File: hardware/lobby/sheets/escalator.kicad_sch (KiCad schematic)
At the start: 2 parts

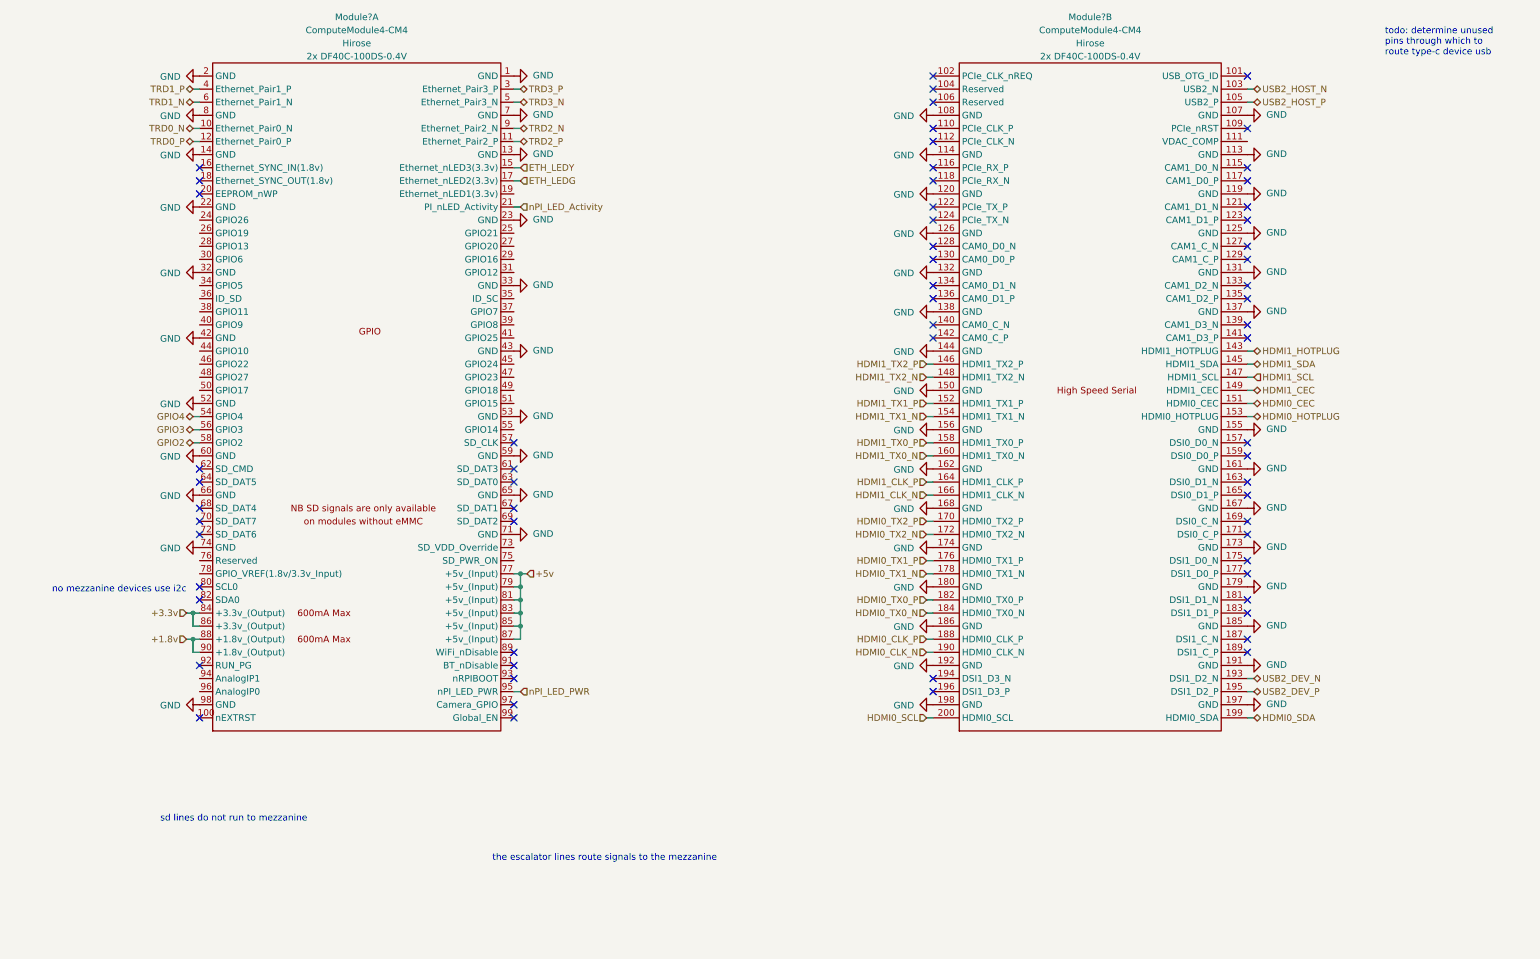
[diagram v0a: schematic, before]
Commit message: start routing mezzanine
making a progress capture before trying to cram a lot of signals onto just one hirose connector...
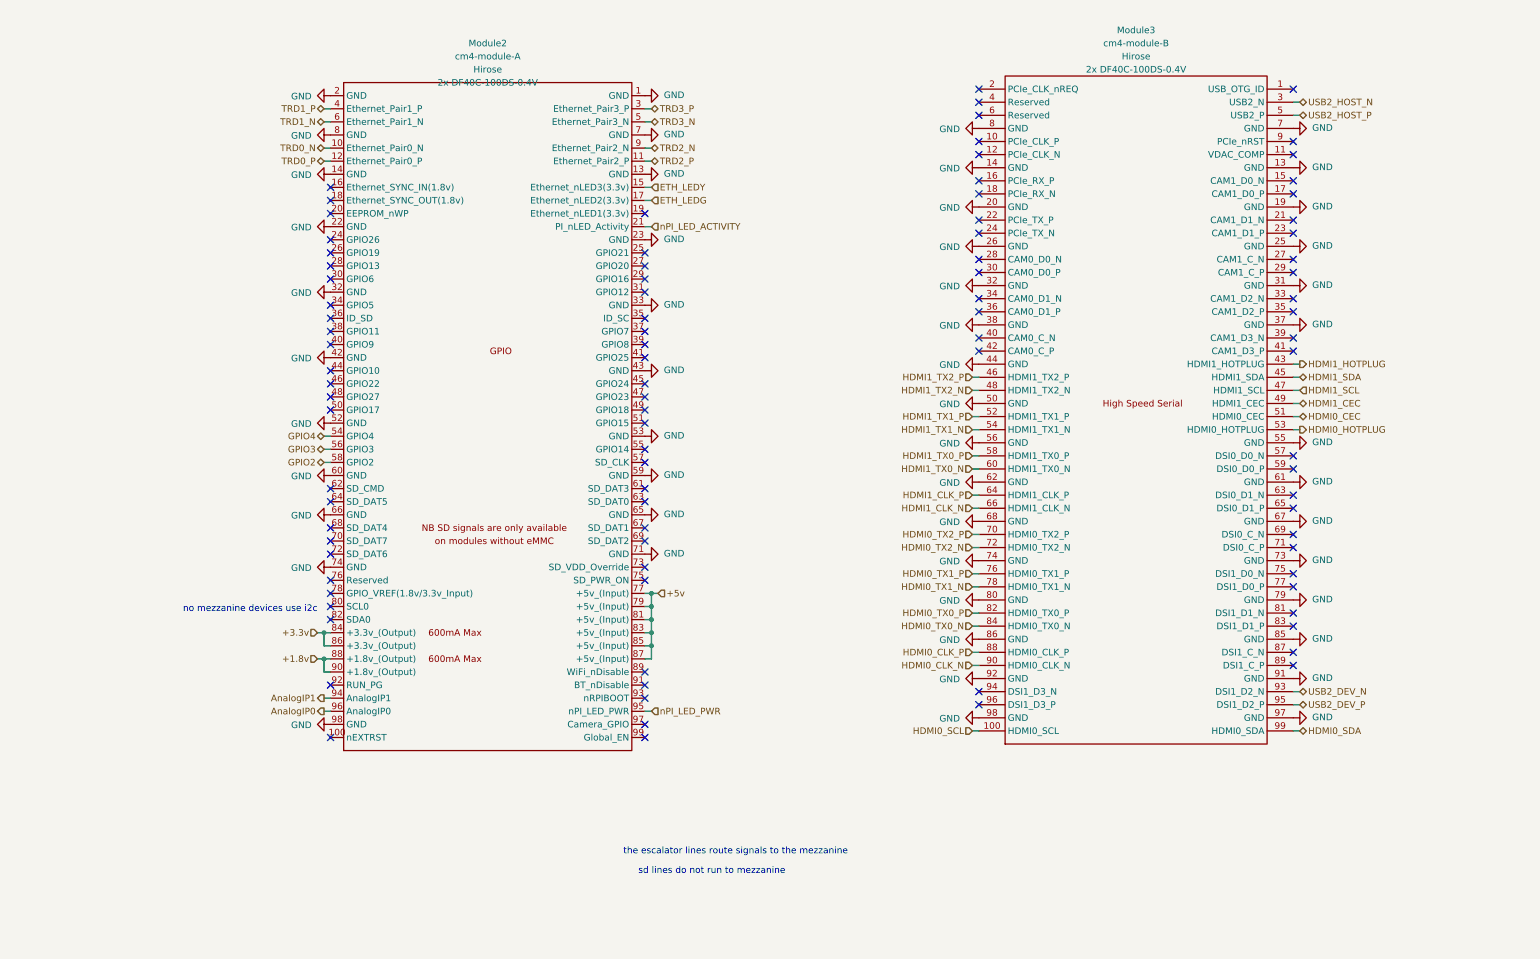
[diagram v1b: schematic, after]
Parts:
- removed Module? (x2): ComputeModule4-CM4, cm4crypto:DF40C-100DS-0.4V(51), symbol cm4crypto:ComputeModule4-CM4
- added Module2: cm4-module-A, cm4crypto:DF40C-100DS-0.4V(51), symbol cm4crypto:cm4-module-A
- added Module3: cm4-module-B, cm4crypto:DF40C-100DS-0.4V(51), symbol cm4crypto:cm4-module-B
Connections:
- net +1.8v: now also Module2.88 (+1.8v_(Output)), Module2.90 (+1.8v_(Output))
- net +3.3v: now also Module2.84 (+3.3v_(Output)), Module2.86 (+3.3v_(Output))
- net +5v: now also Module2.77 (+5v_(Input)), Module2.79 (+5v_(Input)), Module2.81 (+5v_(Input)), Module2.83 (+5v_(Input)), Module2.85 (+5v_(Input)), Module2.87 (+5v_(Input))
- net ETH_LEDG: now also Module2.17 (Ethernet_nLED2(3.3v))
- net ETH_LEDY: now also Module2.15 (Ethernet_nLED3(3.3v))
- net GND: now also Module2.1 (GND), Module2.13 (GND), Module2.14 (GND), Module2.2 (GND), Module2.22 (GND), Module2.23 (GND), Module2.32 (GND), Module2.33 (GND), Module2.42 (GND), Module2.43 (GND), Module2.52 (GND), Module2.53 (GND), Module2.59 (GND), Module2.60 (GND), Module2.65 (GND), Module2.66 (GND), Module2.7 (GND), Module2.71 (GND), Module2.74 (GND), Module2.8 (GND), Module2.98 (GND), Module3.13 (GND), Module3.14 (GND), Module3.19 (GND), Module3.20 (GND), Module3.25 (GND), Module3.26 (GND), Module3.31 (GND), Module3.32 (GND), Module3.37 (GND), Module3.38 (GND), Module3.44 (GND), Module3.50 (GND), Module3.55 (GND), Module3.56 (GND), Module3.61 (GND), Module3.62 (GND), Module3.67 (GND), Module3.68 (GND), Module3.7 (GND), Module3.73 (GND), Module3.74 (GND), Module3.79 (GND), Module3.8 (GND), Module3.80 (GND), Module3.85 (GND), Module3.86 (GND), Module3.91 (GND), Module3.92 (GND), Module3.97 (GND), Module3.98 (GND)
- net GPIO2: now also Module2.58 (GPIO2)
- net GPIO3: now also Module2.56 (GPIO3)
- net GPIO4: now also Module2.54 (GPIO4)
- net HDMI0_CEC: now also Module3.51 (HDMI0_CEC)
- net HDMI0_CLK_N: now also Module3.90 (HDMI0_CLK_N)
- net HDMI0_CLK_P: now also Module3.88 (HDMI0_CLK_P)
- net HDMI0_HOTPLUG: now also Module3.53 (HDMI0_HOTPLUG)
- net HDMI0_SCL: now also Module3.100 (HDMI0_SCL)
- net HDMI0_SDA: now also Module3.99 (HDMI0_SDA)
- net HDMI0_TX0_N: now also Module3.84 (HDMI0_TX0_N)
- net HDMI0_TX0_P: now also Module3.82 (HDMI0_TX0_P)
- net HDMI0_TX1_N: now also Module3.78 (HDMI0_TX1_N)
- net HDMI0_TX1_P: now also Module3.76 (HDMI0_TX1_P)
- net HDMI0_TX2_N: now also Module3.72 (HDMI0_TX2_N)
- net HDMI0_TX2_P: now also Module3.70 (HDMI0_TX2_P)
- net HDMI1_CEC: now also Module3.49 (HDMI1_CEC)
- net HDMI1_CLK_N: now also Module3.66 (HDMI1_CLK_N)
- net HDMI1_CLK_P: now also Module3.64 (HDMI1_CLK_P)
- net HDMI1_HOTPLUG: now also Module3.43 (HDMI1_HOTPLUG)
- net HDMI1_SCL: now also Module3.47 (HDMI1_SCL)
- net HDMI1_SDA: now also Module3.45 (HDMI1_SDA)
- net HDMI1_TX0_N: now also Module3.60 (HDMI1_TX0_N)
- net HDMI1_TX0_P: now also Module3.58 (HDMI1_TX0_P)
- net HDMI1_TX1_N: now also Module3.54 (HDMI1_TX1_N)
- net HDMI1_TX1_P: now also Module3.52 (HDMI1_TX1_P)
- net HDMI1_TX2_N: now also Module3.48 (HDMI1_TX2_N)
- net HDMI1_TX2_P: now also Module3.46 (HDMI1_TX2_P)
- net TRD0_N: now also Module2.10 (Ethernet_Pair0_N)
- net TRD0_P: now also Module2.12 (Ethernet_Pair0_P)
- net TRD1_N: now also Module2.6 (Ethernet_Pair1_N)
- net TRD1_P: now also Module2.4 (Ethernet_Pair1_P)
- net TRD2_N: now also Module2.9 (Ethernet_Pair2_N)
- net TRD2_P: now also Module2.11 (Ethernet_Pair2_P)
- net TRD3_N: now also Module2.5 (Ethernet_Pair3_N)
- net TRD3_P: now also Module2.3 (Ethernet_Pair3_P)
- net USB2_DEV_N: now also Module3.93 (DSI1_D2_N)
- net USB2_DEV_P: now also Module3.95 (DSI1_D2_P)
- net USB2_HOST_N: now also Module3.3 (USB2_N)
- net USB2_HOST_P: now also Module3.5 (USB2_P)
- net nPI_LED_PWR: now also Module2.95 (nPI_LED_PWR)
- new net AnalogIP0: Module2.96 (AnalogIP0)
- new net AnalogIP1: Module2.94 (AnalogIP1)
- new net nPI_LED_ACTIVITY: Module2.21 (PI_nLED_Activity)
- no-connect marks 63 -> 94
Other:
- note removed: "todo: determine unused pins through which to route type-c device usb"

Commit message: sheet refs relative, copied escalator pinout to lobby
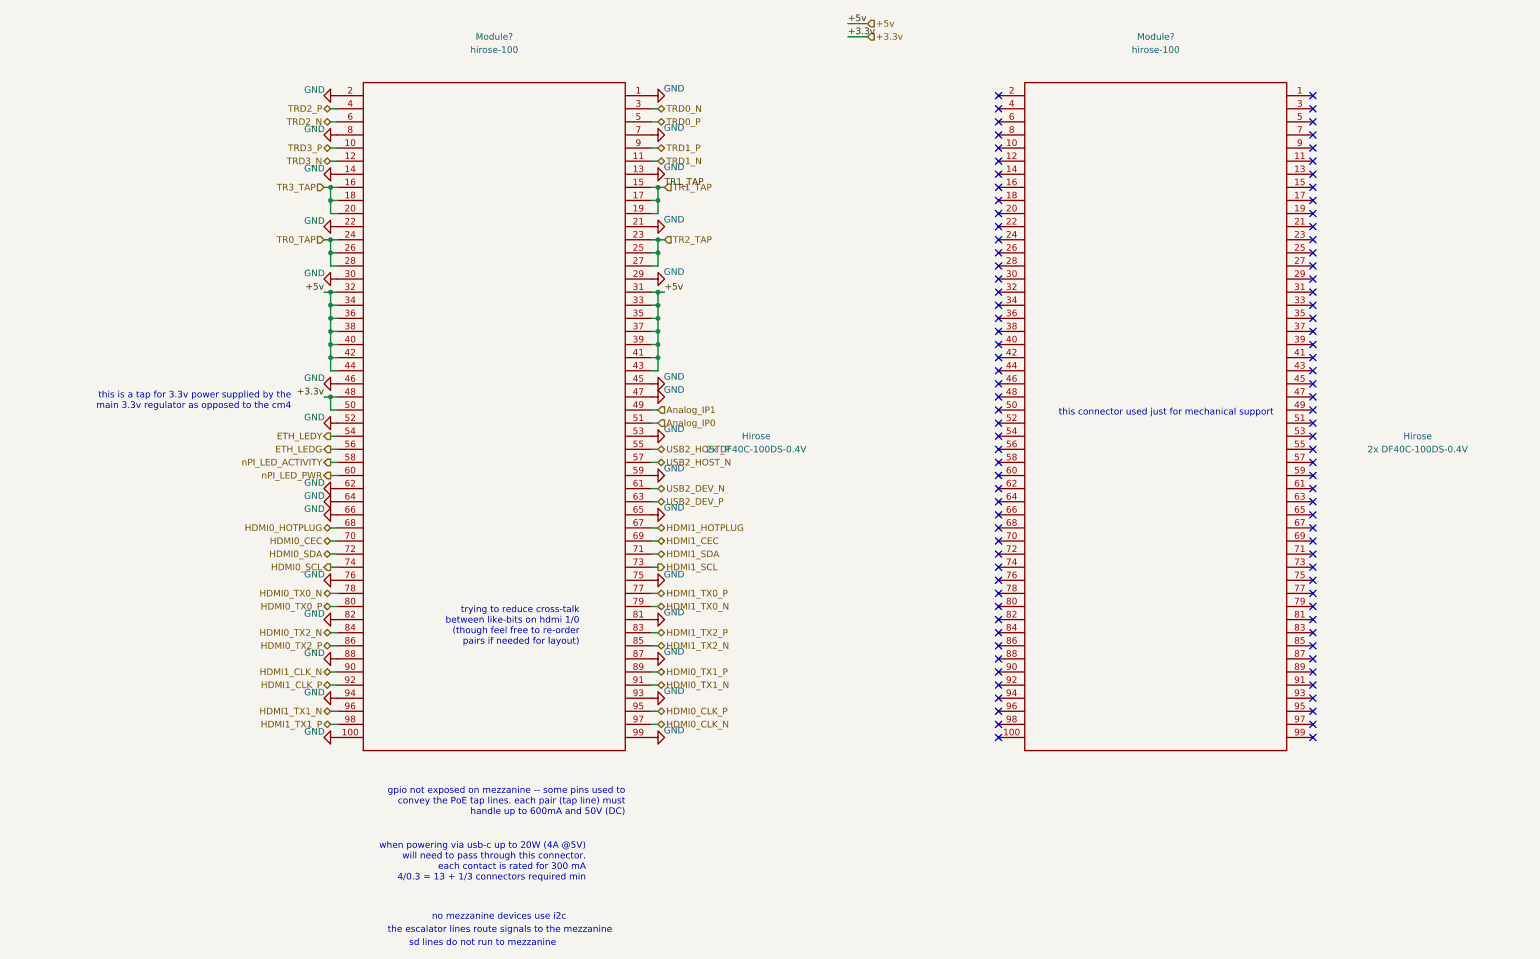
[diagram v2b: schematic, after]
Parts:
- removed Module2: cm4-module-A, cm4crypto:DF40C-100DS-0.4V(51), symbol cm4crypto:cm4-module-A
- removed Module3: cm4-module-B, cm4crypto:DF40C-100DS-0.4V(51), symbol cm4crypto:cm4-module-B
- added Module? (x2): hirose-100, cm4crypto:DF40C-100DP-0.4V(51), symbol cm4crypto:hirose-100
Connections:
- net +3.3v: now also Module?.48, Module?.50
- net +5v: now also Module?.31, Module?.32, Module?.33, Module?.34, Module?.35, Module?.36, Module?.37, Module?.38, Module?.39, Module?.40, Module?.41, Module?.42, Module?.43, Module?.44
- net ETH_LEDG: now also Module?.56
- net ETH_LEDY: now also Module?.54
- net GND: now also Module?.1, Module?.100, Module?.13, Module?.14, Module?.2, Module?.21, Module?.22, Module?.29, Module?.30, Module?.45, Module?.46, Module?.47, Module?.52, Module?.53, Module?.59, Module?.62, Module?.64, Module?.65, Module?.66, Module?.7, Module?.75, Module?.76, Module?.8, Module?.81, Module?.82, Module?.87, Module?.88, Module?.93, Module?.94, Module?.99
- net HDMI0_CEC: now also Module?.70
- net HDMI0_CLK_N: now also Module?.97
- net HDMI0_CLK_P: now also Module?.95
- net HDMI0_HOTPLUG: now also Module?.68
- net HDMI0_SCL: now also Module?.74
- net HDMI0_SDA: now also Module?.72
- net HDMI0_TX0_N: now also Module?.78
- net HDMI0_TX0_P: now also Module?.80
- net HDMI0_TX1_N: now also Module?.91
- net HDMI0_TX1_P: now also Module?.89
- net HDMI0_TX2_N: now also Module?.84
- net HDMI0_TX2_P: now also Module?.86
- net HDMI1_CEC: now also Module?.69
- net HDMI1_CLK_N: now also Module?.90
- net HDMI1_CLK_P: now also Module?.92
- net HDMI1_HOTPLUG: now also Module?.67
- net HDMI1_SCL: now also Module?.73
- net HDMI1_SDA: now also Module?.71
- net HDMI1_TX0_N: now also Module?.79
- net HDMI1_TX0_P: now also Module?.77
- net HDMI1_TX1_N: now also Module?.96
- net HDMI1_TX1_P: now also Module?.98
- net HDMI1_TX2_N: now also Module?.85
- net HDMI1_TX2_P: now also Module?.83
- net TRD0_N: now also Module?.3
- net TRD0_P: now also Module?.5
- net TRD1_N: now also Module?.11
- net TRD1_P: now also Module?.9
- net TRD2_N: now also Module?.6
- net TRD2_P: now also Module?.4
- net TRD3_N: now also Module?.12
- net TRD3_P: now also Module?.10
- net USB2_DEV_N: now also Module?.61
- net USB2_DEV_P: now also Module?.63
- net USB2_HOST_N: now also Module?.57
- net USB2_HOST_P: now also Module?.55
- net nPI_LED_ACTIVITY: now also Module?.58
- net nPI_LED_PWR: now also Module?.60
- new net Analog_IP0: Module?.51
- new net Analog_IP1: Module?.49
- new net TR0_TAP: Module?.24, Module?.26, Module?.28
- new net TR1_TAP: Module?.15, Module?.17, Module?.19
- new net TR2_TAP: Module?.23, Module?.25, Module?.27
- new net TR3_TAP: Module?.16, Module?.18, Module?.20
- no-connect marks 94 -> 100
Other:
- note added: "gpio not exposed on mezzanine -- some pins used to convey the PoE tap lines. each pair (tap line) must handle up to 600mA and 50V (DC)"
- note added: "this connector used just for mechanical support"
- note added: "this is a tap for 3.3v power supplied by the main 3.3v regulator as opposed to the cm4"
- note added: "trying to reduce cross-talk between like-bits on hdmi 1/0 (though feel free to re-order pairs if needed for layout)"
- note added: "when powering via usb-c up to 20W (4A @5V) will need to pass through this connector. each contact is rated for 300 mA 4/0.3 = 13 + 1/3 connectors required min"
